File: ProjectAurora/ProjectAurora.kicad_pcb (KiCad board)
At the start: 4 copper layers, 36 x 36 mm, 84 parts, among them IC1 IS31FL3237-QFLS4-TR, IC2 LSM303AGRTR, IC3 BQ25185DLHR, IC4 MAX17048G+T10, IC5 TPS63900DSKR, J1 USB_C_Receptacle_USB2.0_14P, U1 STM32U031K8Ux, U2 CP2102N-Axx-xQFN20, U3 TPD2EUSB30A, U4 TMP1075DSG, Y1 ABS07-32.768KHZ-T

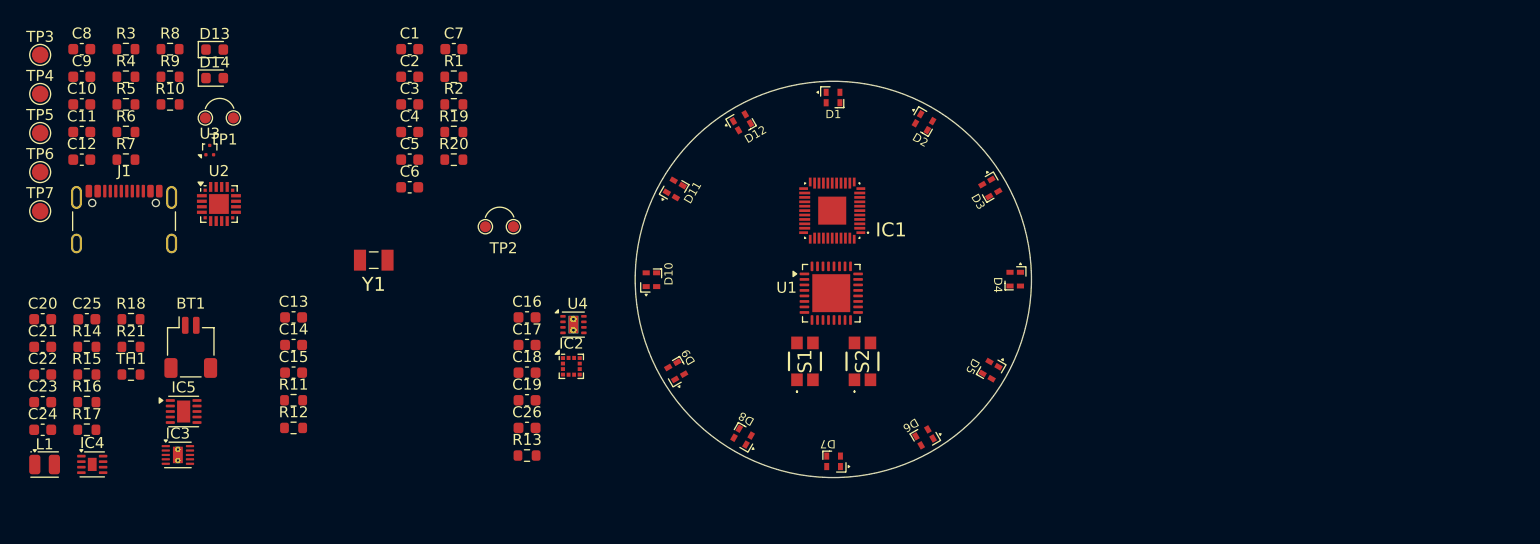
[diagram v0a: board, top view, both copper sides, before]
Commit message: Prototype Board Layout Done
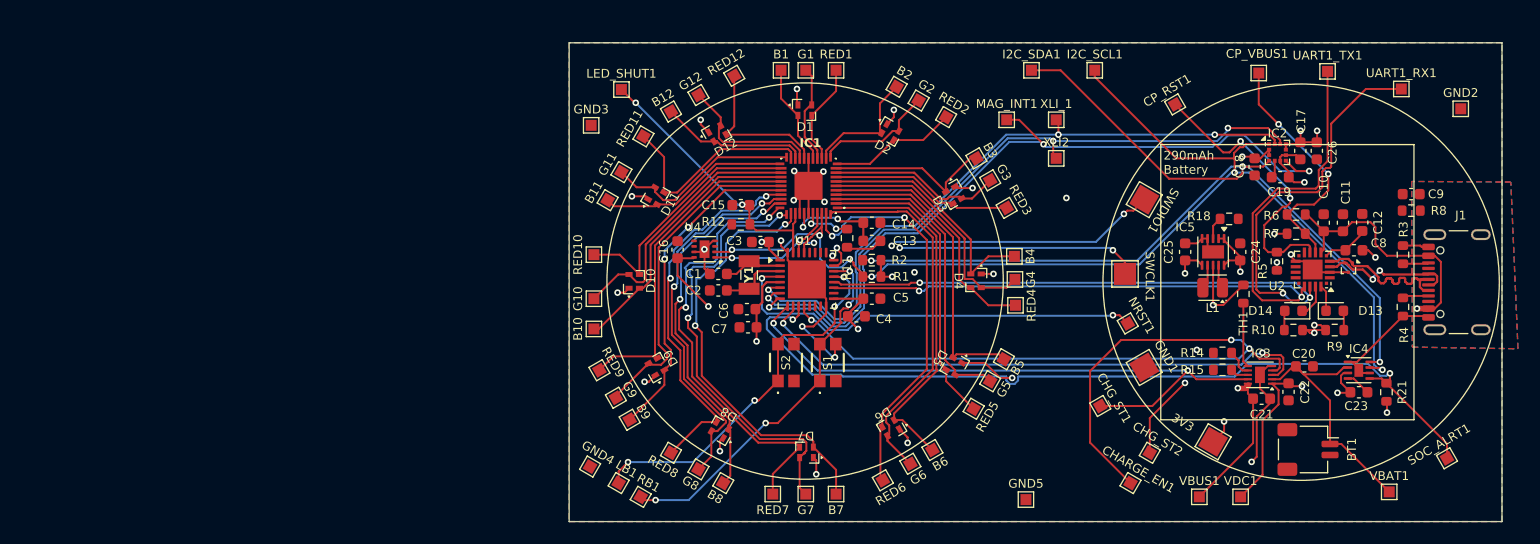
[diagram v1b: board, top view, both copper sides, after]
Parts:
- removed R13: 5K, Resistor_SMD:R_0603_1608Metric
- removed R16, R17, R19, R20: 10K, Resistor_SMD:R_0603_1608Metric
- removed TP1, TP2: TestPoint_2Pole, Test-Point-Jumper:2-Pin-Jumper
- added B1: TestPoint, TestPoint:TestPoint_Pad_1.0x1.0mm, F.Cu at (135.2, 81.0)
- added B10: TestPoint, TestPoint:TestPoint_Pad_1.0x1.0mm, F.Cu at (118.2, 104.5)
- added B11: TestPoint, TestPoint:TestPoint_Pad_1.0x1.0mm, F.Cu at (119.5, 92.8)
- added B12: TestPoint, TestPoint:TestPoint_Pad_1.0x1.0mm, F.Cu at (125.2, 84.8)
- added B2: TestPoint, TestPoint:TestPoint_Pad_1.0x1.0mm, F.Cu at (145.8, 82.5)
- added B3: TestPoint, TestPoint:TestPoint_Pad_1.0x1.0mm, F.Cu at (153.0, 89.0)
- added B4: TestPoint, TestPoint:TestPoint_Pad_1.0x1.0mm, F.Cu at (156.4, 97.9)
- added B5: TestPoint, TestPoint:TestPoint_Pad_1.0x1.0mm, F.Cu at (155.5, 107.2)
- added B6: TestPoint, TestPoint:TestPoint_Pad_1.0x1.0mm, F.Cu at (149.0, 115.5)
- added B7: `, TestPoint:TestPoint_Pad_1.0x1.0mm, F.Cu at (140.2, 119.5)
- added B8: TestPoint, TestPoint:TestPoint_Pad_1.0x1.0mm, F.Cu at (130.0, 118.5)
- added B9: TestPoint, TestPoint:TestPoint_Pad_1.0x1.0mm, F.Cu at (121.5, 112.8)
- added CHARGE_EN1: TestPoint, TestPoint:TestPoint_Pad_1.0x1.0mm, F.Cu at (167.0, 118.5)
- added CHG_ST1: TestPoint, TestPoint:TestPoint_Pad_1.0x1.0mm, F.Cu at (164.2, 111.5)
- added CHG_ST2: TestPoint, TestPoint:TestPoint_Pad_1.0x1.0mm, F.Cu at (168.8, 115.8)
- added CP_RST1: TestPoint, TestPoint:TestPoint_Pad_1.0x1.0mm, F.Cu at (171.1, 84.1)
- added CP_VBUS1: TestPoint, TestPoint:TestPoint_Pad_1.0x1.0mm, F.Cu at (178.7, 81.2)
- added G1: TestPoint, TestPoint:TestPoint_Pad_1.0x1.0mm, F.Cu at (137.5, 81.0)
- added G10: TestPoint, TestPoint:TestPoint_Pad_1.0x1.0mm, F.Cu at (118.2, 101.8)
- added G11: TestPoint, TestPoint:TestPoint_Pad_1.0x1.0mm, F.Cu at (120.8, 90.2)
- added G12: TestPoint, TestPoint:TestPoint_Pad_1.0x1.0mm, F.Cu at (127.8, 83.2)
- added G2: TestPoint, TestPoint:TestPoint_Pad_1.0x1.0mm, F.Cu at (147.8, 83.8)
- added G3: TestPoint, TestPoint:TestPoint_Pad_1.0x1.0mm, F.Cu at (154.2, 91.0)
- added G4: TestPoint, TestPoint:TestPoint_Pad_1.0x1.0mm, F.Cu at (156.5, 100.0)
- added G5: TestPoint, TestPoint:TestPoint_Pad_1.0x1.0mm, F.Cu at (154.2, 109.2)
- added G6: TestPoint, TestPoint:TestPoint_Pad_1.0x1.0mm, F.Cu at (147.0, 116.8)
- added G7: TestPoint, TestPoint:TestPoint_Pad_1.0x1.0mm, F.Cu at (137.5, 119.5)
- added G8: TestPoint, TestPoint:TestPoint_Pad_1.0x1.0mm, F.Cu at (127.8, 117.2)
- added G9: TestPoint, TestPoint:TestPoint_Pad_1.0x1.0mm, F.Cu at (120.2, 110.8)
- added GND2: TestPoint, TestPoint:TestPoint_Pad_1.0x1.0mm, F.Cu at (197.0, 84.5)
- added GND3: TestPoint, TestPoint:TestPoint_Pad_1.0x1.0mm, F.Cu at (118.0, 86.0)
- added GND4: TestPoint, TestPoint:TestPoint_Pad_1.0x1.0mm, F.Cu at (117.9, 117.0)
- added GND5: TestPoint, TestPoint:TestPoint_Pad_1.0x1.0mm, F.Cu at (157.5, 120.0)
- added I2C_SCL1: TestPoint, TestPoint:TestPoint_Pad_1.0x1.0mm, F.Cu at (163.8, 81.0)
- added I2C_SDA1: TestPoint, TestPoint:TestPoint_Pad_1.0x1.0mm, F.Cu at (158.0, 81.0)
- added LB1: TestPoint, TestPoint:TestPoint_Pad_1.0x1.0mm, F.Cu at (120.5, 118.5)
- added LED_SHUT1: TestPoint, TestPoint:TestPoint_Pad_1.0x1.0mm, F.Cu at (120.8, 82.8)
- added MAG_INT1: TestPoint, TestPoint:TestPoint_Pad_1.0x1.0mm, F.Cu at (155.8, 85.5)
- added RB1: TestPoint, TestPoint:TestPoint_Pad_1.0x1.0mm, F.Cu at (122.5, 119.8)
- added RED1: TestPoint, TestPoint:TestPoint_Pad_1.0x1.0mm, F.Cu at (140.2, 81.0)
- added RED10: TestPoint, TestPoint:TestPoint_Pad_1.0x1.0mm, F.Cu at (118.2, 97.8)
- added RED11: TestPoint, TestPoint:TestPoint_Pad_1.0x1.0mm, F.Cu at (122.8, 87.0)
- added RED12: TestPoint, TestPoint:TestPoint_Pad_1.0x1.0mm, F.Cu at (131.0, 81.5)
- added RED2: TestPoint, TestPoint:TestPoint_Pad_1.0x1.0mm, F.Cu at (150.2, 85.2)
- added RED3: TestPoint, TestPoint:TestPoint_Pad_1.0x1.0mm, F.Cu at (155.8, 93.5)
- added RED4: TestPoint, TestPoint:TestPoint_Pad_1.0x1.0mm, F.Cu at (156.6, 102.3)
- added RED5: TestPoint, TestPoint:TestPoint_Pad_1.0x1.0mm, F.Cu at (152.8, 111.8)
- added RED6: TestPoint, TestPoint:TestPoint_Pad_1.0x1.0mm, F.Cu at (144.5, 118.2)
- added RED7: TestPoint, TestPoint:TestPoint_Pad_1.0x1.0mm, F.Cu at (134.5, 119.5)
- added RED8: TestPoint, TestPoint:TestPoint_Pad_1.0x1.0mm, F.Cu at (125.2, 115.8)
- added RED9: TestPoint, TestPoint:TestPoint_Pad_1.0x1.0mm, F.Cu at (118.8, 108.2)
- added SOC_ALRT1: TestPoint, TestPoint:TestPoint_Pad_1.0x1.0mm, F.Cu at (195.8, 116.2)
- added UART1_RX1: TestPoint, TestPoint:TestPoint_Pad_1.0x1.0mm, F.Cu at (191.6, 82.7)
- added UART1_TX1: TestPoint, TestPoint:TestPoint_Pad_1.0x1.0mm, F.Cu at (184.9, 81.1)
- added VBAT1: TestPoint, TestPoint:TestPoint_Pad_1.0x1.0mm, F.Cu at (190.5, 119.3)
- added VBUS1: TestPoint, TestPoint:TestPoint_Pad_1.0x1.0mm, F.Cu at (173.2, 119.8)
- added VDC1: TestPoint, TestPoint:TestPoint_Pad_1.0x1.0mm, F.Cu at (177.0, 119.8)
- added XLI2: TestPoint, TestPoint:TestPoint_Pad_1.0x1.0mm, F.Cu at (160.2, 89.0)
- added XLI_1: TestPoint, TestPoint:TestPoint_Pad_1.0x1.0mm, F.Cu at (160.2, 85.5)
- 3V3: renamed from TP3; footprint TestPoint:TestPoint_Pad_D1.5mm -> TestPoint:TestPoint_Pad_2.0x2.0mm
- GND1: renamed from TP7; footprint TestPoint:TestPoint_Pad_D1.5mm -> TestPoint:TestPoint_Pad_2.0x2.0mm
- NRST1: renamed from TP6; footprint TestPoint:TestPoint_Pad_D1.5mm -> TestPoint:TestPoint_Pad_1.0x1.0mm
- SWCLK1: renamed from TP5; footprint TestPoint:TestPoint_Pad_D1.5mm -> TestPoint:TestPoint_Pad_2.0x2.0mm
- SWDIO1: renamed from TP4; footprint TestPoint:TestPoint_Pad_D1.5mm -> TestPoint:TestPoint_Pad_2.0x2.0mm
- moved J1 122.3 mm to (197.8, 100.2), turned to 90 degrees
- moved C9 121.2 mm to (192.5, 92.2)
- moved C23 119.6 mm to (187.8, 110.2)
- moved R4 117.9 mm to (191.8, 102.5), turned to -90 degrees
- moved R3 117.5 mm to (191.8, 97.8), turned to 90 degrees
- moved C8 117.0 mm to (187.3, 97.3), turned to 180 degrees
- moved C12 116.5 mm to (188.1, 94.8), turned to -90 degrees
- moved IC4 115.4 mm to (187.7, 108.2)
- moved C11 114.9 mm to (186.3, 94.8), turned to -90 degrees
- moved C20 114.7 mm to (182.8, 107.9)
- moved R21 114.1 mm to (190.2, 110.2), turned to -90 degrees
- moved R8 113.7 mm to (192.5, 93.8)
- moved C10 113.3 mm to (184.5, 94.8), turned to -90 degrees
- moved C22 113.2 mm to (181.4, 110.2), turned to 90 degrees
- moved 3V3 112.2 mm to (174.5, 114.8), turned to -30 degrees
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- renumbered D9 to D10, D8 to D11, D7 to D12, D12 to D7, D11 to D8, D10 to D9
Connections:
- C16 pad 2: +3.3V -> +3V3
- C23 pad 1: +3.3V -> +3V3
- D1 pad 2: /LEDs & Controller/OUT3 -> /LEDs & Controller/OUT18
- D1 pad 3: /LEDs & Controller/OUT2 -> /LEDs & Controller/OUT17
- D1 pad 4: /LEDs & Controller/OUT1 -> /LEDs & Controller/OUT16
- D2 pad 2: /LEDs & Controller/OUT6 -> /LEDs & Controller/OUT15
- D2 pad 3: /LEDs & Controller/OUT5 -> /LEDs & Controller/OUT14
- D2 pad 4: /LEDs & Controller/OUT4 -> /LEDs & Controller/OUT13
- D3 pad 2: /LEDs & Controller/OUT9 -> /LEDs & Controller/OUT12
- D3 pad 3: /LEDs & Controller/OUT8 -> /LEDs & Controller/OUT11
- D3 pad 4: /LEDs & Controller/OUT7 -> /LEDs & Controller/OUT10
- D4 pad 2: /LEDs & Controller/OUT12 -> /LEDs & Controller/OUT9
- D4 pad 3: /LEDs & Controller/OUT11 -> /LEDs & Controller/OUT8
- D4 pad 4: /LEDs & Controller/OUT10 -> /LEDs & Controller/OUT7
- D5 pad 2: /LEDs & Controller/OUT15 -> /LEDs & Controller/OUT6
- D5 pad 3: /LEDs & Controller/OUT14 -> /LEDs & Controller/OUT5
- D5 pad 4: /LEDs & Controller/OUT13 -> /LEDs & Controller/OUT4
- D6 pad 2: /LEDs & Controller/OUT18 -> /LEDs & Controller/OUT3
- D6 pad 3: /LEDs & Controller/OUT17 -> /LEDs & Controller/OUT2
- D6 pad 4: /LEDs & Controller/OUT16 -> /LEDs & Controller/OUT1
- IC4 pad 3: +3.3V -> +3V3
- U1 pad 28: /LED_SHUTDOWN -> unconnected-(U1-PB5-Pad28)
- U1 pad 31: unconnected-(U1-PF3-Pad31) -> /LED_SHUTDOWN
- U3 pad 1: /USB & Debug/D+ -> /USB & Debug/D-
- U3 pad 2: /USB & Debug/D- -> /USB & Debug/D+
- U4 pad 3: /TEMP_ALRT -> unconnected-(U4-ALERT-Pad3)
- U4 pad 8: +3.3V -> +3V3
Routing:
- net /I2C_SDA: track 0.00 -> 109.6 mm, vias 0 -> 6
- net /I2C1_SCL: track 0.00 -> 108.3 mm, vias 0 -> 6
- net GND: track 0.00 -> 85.3 mm, vias 0 -> 17
- net +3V3: track 0.00 -> 81.7 mm, vias 0 -> 29
- net /USART1_MCU_RX: track 0.00 -> 78.4 mm, vias 0 -> 3
- net /~{SOC_ALRT}: track 0.00 -> 77.1 mm, vias 0 -> 2
- net /~{CHARGE_EN}: track 0.00 -> 75.6 mm, vias 0 -> 3
- net /USART1_MCU_TX: track 0.00 -> 74.0 mm, vias 0 -> 2
- net /MAG_INT: track 0.00 -> 69.7 mm, vias 0 -> 3
- net /CHARGE_STAT_2: track 0.00 -> 67.8 mm, vias 0 -> 3
- net /XL_INT_2: track 0.00 -> 61.7 mm, vias 0 -> 3
- net /XL_INT_1: track 0.00 -> 60.1 mm, vias 0 -> 3
- net VBUS: track 0.00 -> 57.6 mm, vias 0 -> 2
- net /CHARGE_STAT_1: track 0.00 -> 56.8 mm, vias 0 -> 2
- net /LEDs & Controller/OUT34: track 0.00 -> 40.8 mm, vias 0 -> 2
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- added copper zone on In2.Cu, net +3V3
- added copper zone on B.Cu, net Earth
- added copper zone on F.Cu, net Earth
- added copper zone on In1.Cu, net Earth
- added copper zone on In2.Cu, net Earth
- added copper zone on B.Cu, net GND
- added copper zone on F.Cu, net GND
- added copper zone on In1.Cu, net GND
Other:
- board size 36 x 36 mm -> 84.8 x 43.5 mm
- board text added: "290mAh Battery"

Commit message: Prototype Board Ready for Ordering
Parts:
- added G***: LOGO, LOGO, F.Cu at (131.3, 107.8)
- added G***: LOGO, LOGO, F.Cu at (159.0, 113.9)
- R5: value 10K -> 1K
- renumbered D2 to D1, D11 to D10, D12 to D11, D1 to D12, D3 to D2, D4 to D3, D5 to D4, D6 to D5, D7 to D6, D8 to D7, D9 to D8, D10 to D9
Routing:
- net GND: vias 17 -> 19
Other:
- board text added: "Project Aurora Rev. Proto. 1"

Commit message: Setting Up the Firmware
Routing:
- net GND: vias 19 -> 114
